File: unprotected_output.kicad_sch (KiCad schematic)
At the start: 0 parts

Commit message: [WIP] unprotected front-end sheet with components
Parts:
- added J4: Bus_PCI_Express_x1, Connector_PCBEdge:BUS_PCIexpress_x1, symbol Connectors:Bus_PCI_Express_x1
- added U10, U8, U9: LFS0108, Package_SO:TSSOP-20_4.4x6.5mm_P0.65mm, symbol Logic_Level_Translator:LSF0108
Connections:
- net P0: now also U8.19 (refB)
- net P1: now also U8.17 (B2)
- net P10: now also U9.16 (B3)
- net P11: now also U9.15 (B4)
- net P12: now also U9.14 (B5)
- net P13: now also U9.13 (B6)
- net P14: now also U9.12 (B7)
- net P15: now also U9.11 (B8)
- net P16: now also U10.19 (refB)
- net P17: now also U10.17 (B2)
- net P18: now also U10.16 (B3)
- net P19: now also U10.15 (B4)
- net P2: now also U8.16 (B3)
- net P20: now also U10.14 (B5)
- net P21: now also U10.13 (B6)
- net P22: now also U10.12 (B7)
- net P23: now also U10.11 (B8)
- net P3: now also U8.15 (B4)
- net P4: now also U8.14 (B5)
- net P5: now also U8.13 (B6)
- net P6: now also U8.12 (B7)
- net P7: now also U8.11 (B8)
- net P8: now also U9.19 (refB)
- net P9: now also U9.17 (B2)
- new net +3.3V: U10.19 (refB), U8.19 (refB), U9.19 (refB)
- new net CH00: U8.3 (A1)
- new net CH01: U8.4 (A2)
- new net CH02: U8.5 (A3)
- new net CH03: U8.6 (A4)
- new net CH04: U8.7 (A5)
- new net CH05: U8.8 (A6)
- new net CH06: U8.9 (A7)
- new net CH07: U8.10 (A8)
- new net CH08: U9.3 (A1)
- new net CH09: U9.4 (A2)
- new net CH10: U9.5 (A3)
- new net CH11: U9.6 (A4)
- new net CH12: U9.7 (A5)
- new net CH13: U9.8 (A6)
- new net CH14: U9.9 (A7)
- new net CH15: U9.10 (A8)
- new net CH16: U10.3 (A1)
- new net CH17: U10.4 (A2)
- new net CH18: U10.5 (A3)
- new net CH19: U10.6 (A4)
- new net CH20: U10.7 (A5)
- new net CH21: U10.8 (A6)
- new net CH22: U10.9 (A7)
- new net CH23: U10.10 (A8)
- new net GND: U10.1 (GND), U8.1 (GND), U9.1 (GND)
- new net TXSOE: U10.20 (EN), U8.20 (EN), U9.20 (EN)
- new net Vdrive: U10.2 (refA), U8.2 (refA), U9.2 (refA)
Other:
- note added: "Shift Level 0,8~5 V LSF0108"

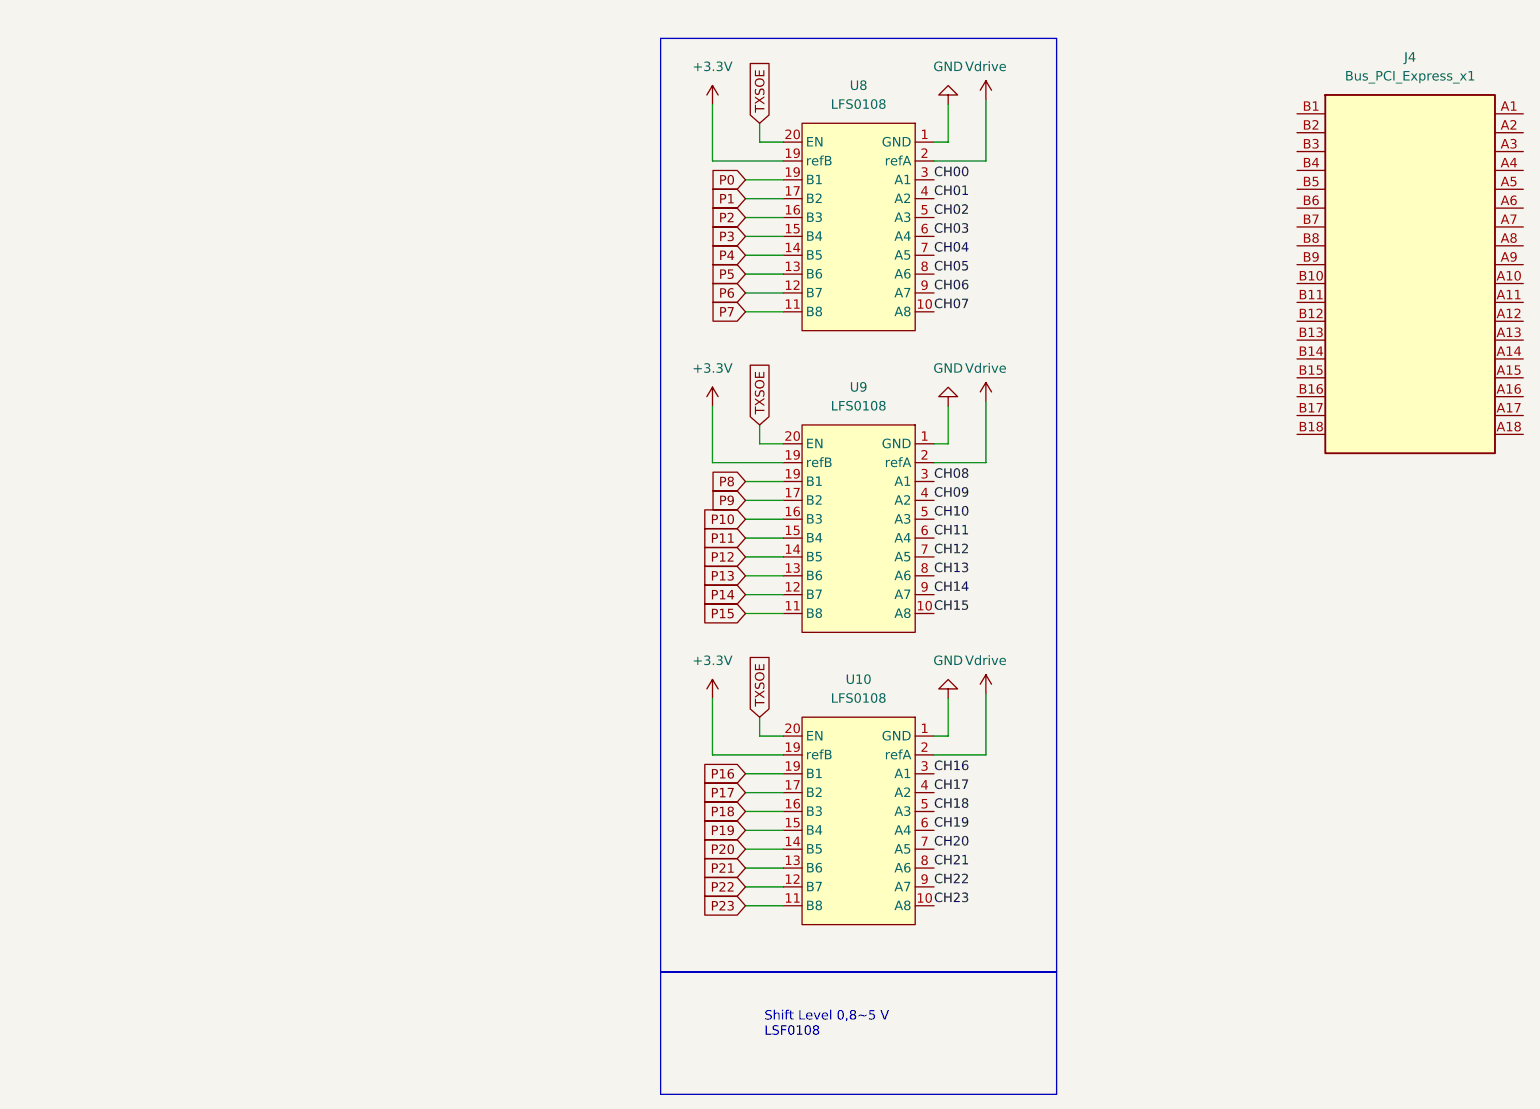
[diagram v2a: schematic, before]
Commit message: [WIP] pcb design with minor fixes in schema to have cleanest routing
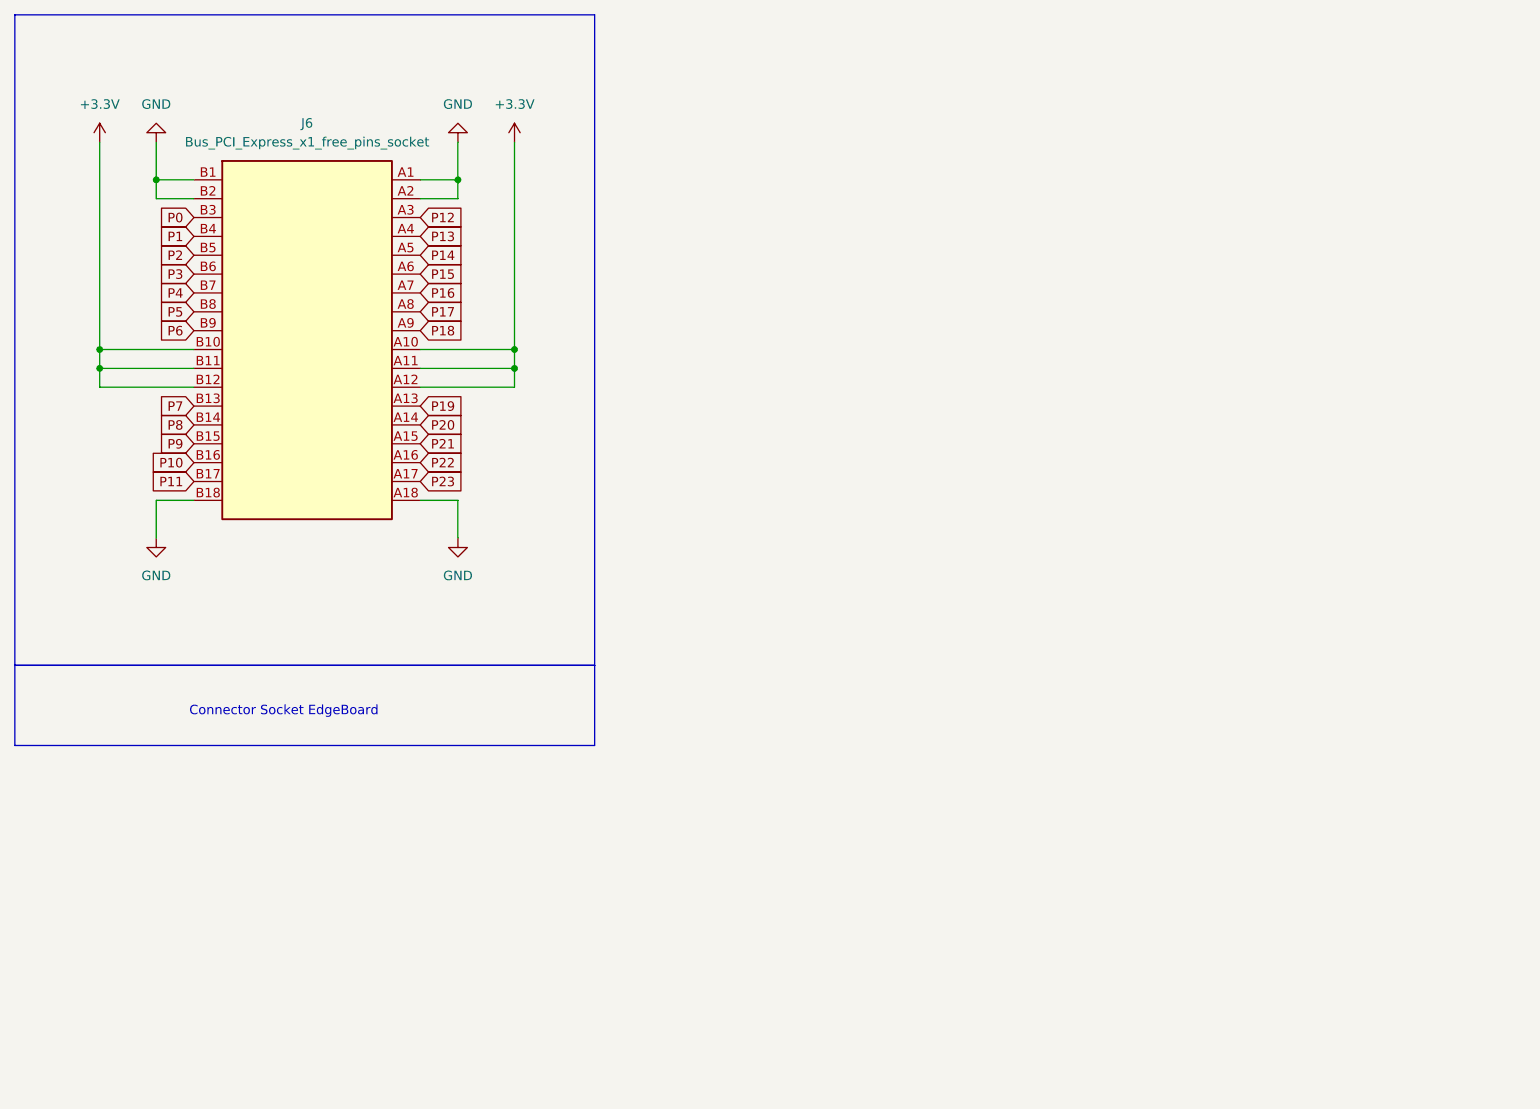
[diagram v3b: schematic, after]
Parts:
- removed J4: Bus_PCI_Express_x1, Connector_PCBEdge:BUS_PCIexpress_x1, symbol Connectors:Bus_PCI_Express_x1
- removed U10, U8, U9: LFS0108, Package_SO:TSSOP-20_4.4x6.5mm_P0.65mm, symbol Logic_Level_Translator:LSF0108
- added J6: Bus_PCI_Express_x1_free_pins_socket, Connector_EdgeBoard:PCI-E_x1_Socket_UMAX_3091-10100T, symbol Connectors:Bus_PCI_Express_x1_free_pins_socket
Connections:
- net +3.3V: now also J6.A10, J6.A11, J6.A12, J6.B10, J6.B11, J6.B12
- net GND: now also J6.A1, J6.A18, J6.A2, J6.B1, J6.B18, J6.B2
- net P0: now also J6.B3
- net P1: now also J6.B4
- net P10: now also J6.B16
- net P11: now also J6.B17
- net P12: now also J6.A3
- net P13: now also J6.A4
- net P14: now also J6.A5
- net P15: now also J6.A6
- net P16: now also J6.A7
- net P17: now also J6.A8
- net P18: now also J6.A9
- net P19: now also J6.A13
- net P2: now also J6.B5
- net P20: now also J6.A14
- net P21: now also J6.A15
- net P22: now also J6.A16
- net P23: now also J6.A17
- net P3: now also J6.B6
- net P4: now also J6.B7
- net P5: now also J6.B8
- net P6: now also J6.B9
- net P7: now also J6.B13
- net P8: now also J6.B14
- net P9: now also J6.B15
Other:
- note added: "Connector Socket EdgeBoard"
- note removed: "Shift Level 0,8~5 V LSF0108"
